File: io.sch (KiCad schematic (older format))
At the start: 115 parts, among them P1 OUT_GND, P10 INJ-CPU, P11 INJECTORS, P12 LSD-CPU, P13 LSDS, P2 TRIG-cpu, P3 DIG-CPU, P4 IN-CPU, P5 CPU_PWR, P6 TRIG-IN, P7 DIG-IN, P8 IGNITION, P9 PWR_IN, Q1 MOSFET, Q2 MOSFET, Q3 MOSFET, Q4 MOSFET, Q5 MOSFET, Q6 MOSFET, Q7 MOSFET, Q8 MOSFET, U1 LM2940, U10 BTF3080EJ, U11 BTF3080EJ, U12 MIC4469, U13 MIC4469, U2 MIC4469, U3 MAX9926UAEE+, U4 BTF3080EJ, U5 BTF3080EJ, U6 BTF3080EJ, U7 BTF3080EJ, U8 BTF3080EJ, U9 BTF3080EJ

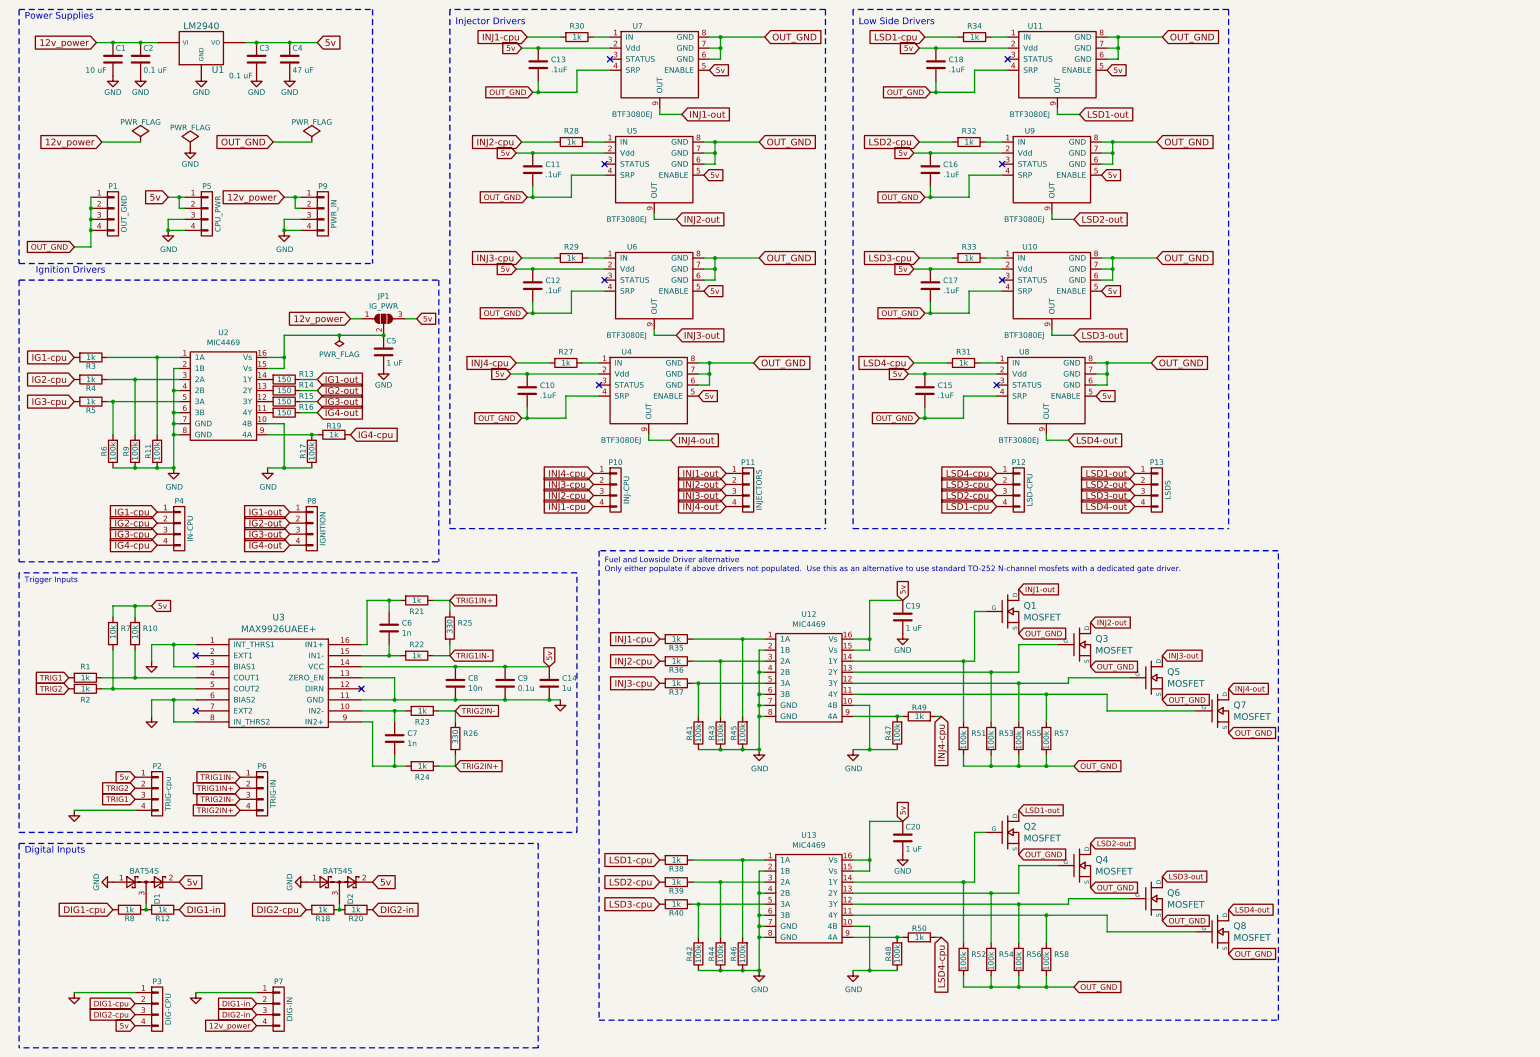
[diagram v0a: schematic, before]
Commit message: Switch to a gate driver and normal power mosfets
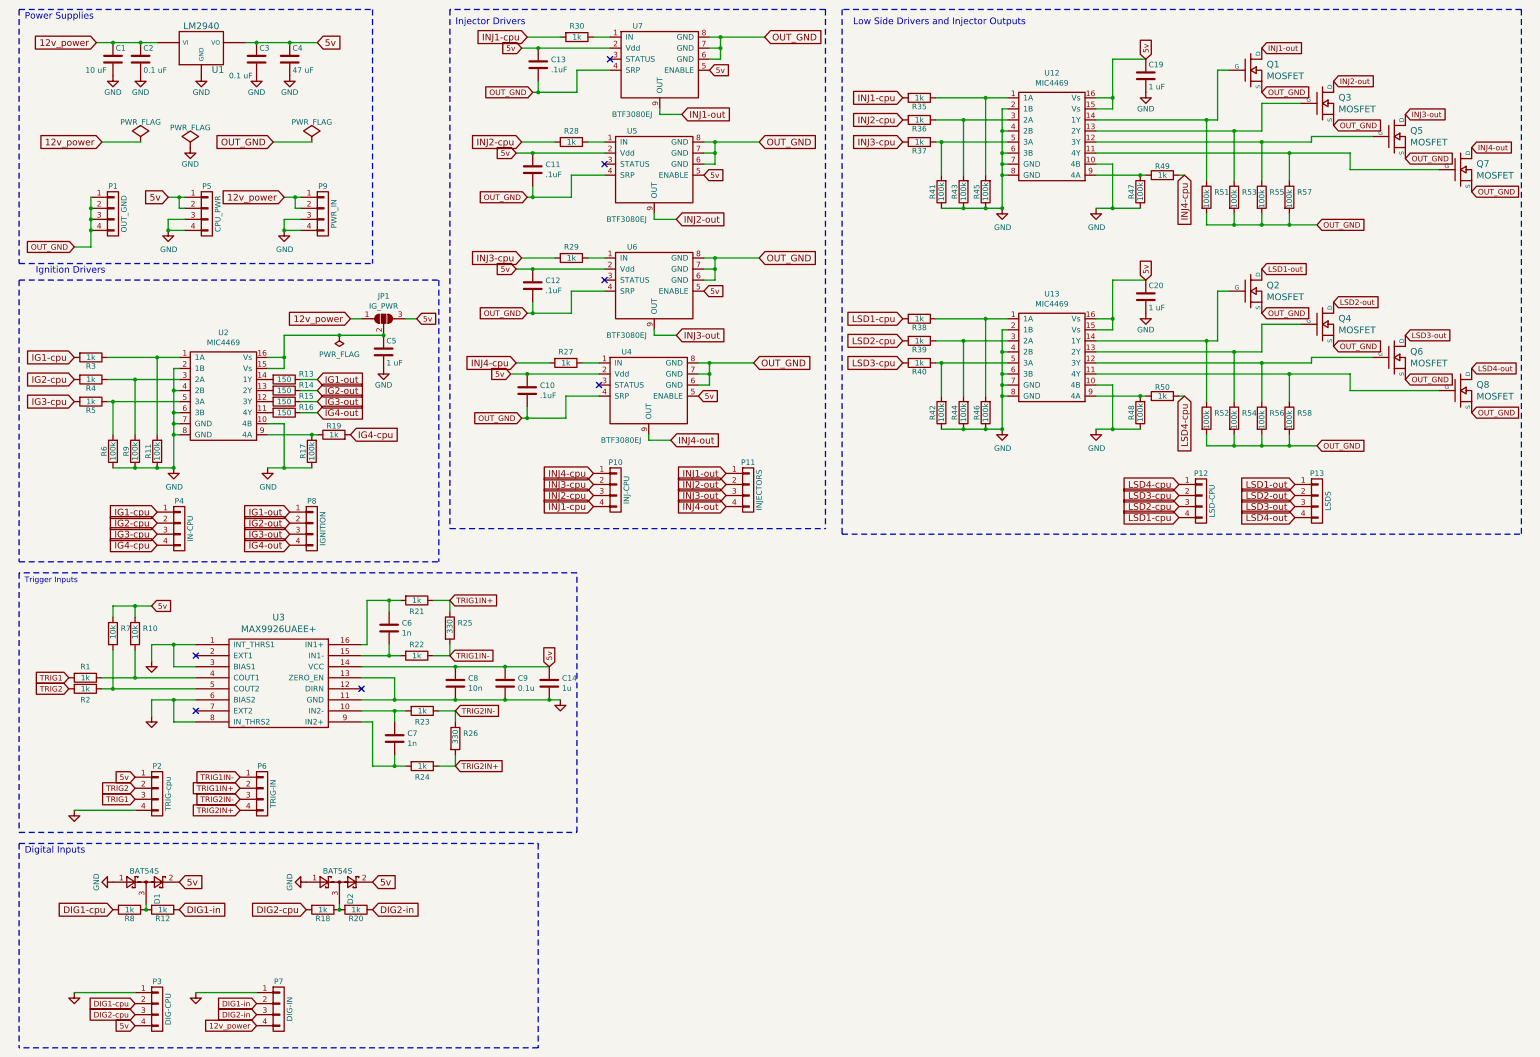
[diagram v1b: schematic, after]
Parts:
- removed C15, C16, C17, C18: .1uF, Capacitor_SMD:C_0805_2012Metric_Pad1.18x1.45mm_HandSolder, symbol analog-rescue:C
- removed R31, R32, R33, R34: 1k, Resistor_SMD:R_0805_2012Metric_Pad1.20x1.40mm_HandSolder, symbol io-rescue:R-io-rescue
- removed U10, U11, U8, U9: BTF3080EJ, Package_SO:Infineon_PG-DSO-8-27_3.9x4.9mm_EP2.65x3mm, symbol io-rescue:BTF3080EJ
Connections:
- no-connect marks 11 -> 7
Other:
- note added: "Low Side Drivers and Injector Outputs"
- note removed: "Fuel and Lowside Driver alternative\nOnly either populate if above drivers not populated. Use this as an alternative to use standard TO-252 N-channel mosfets with a dedicated gate driver."
- note removed: "Low Side Drivers"
- moved on the sheet: C19, C20, P12, P13, Q1, Q2, Q3, Q4, Q5, Q6, Q7, Q8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
